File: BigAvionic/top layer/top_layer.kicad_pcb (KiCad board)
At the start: 4 copper layers, 68 x 68 mm, 28 parts, among them J1 Conn_01x08, J2 Conn_Coaxial, J3 Conn_01x04, U1 NEO-M9N-00B, U2 MMC5983MA

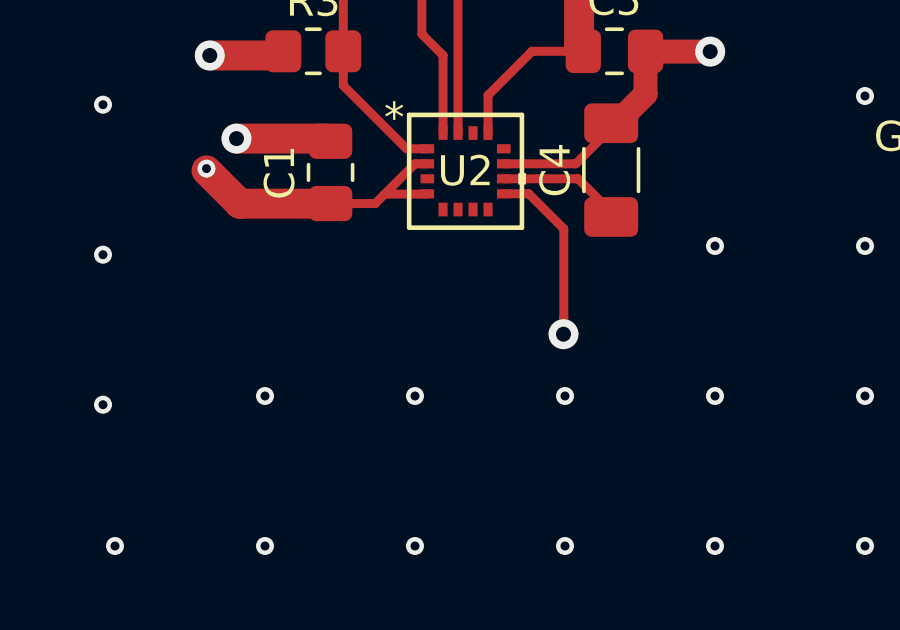
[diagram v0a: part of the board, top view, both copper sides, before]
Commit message: edit some in MCU for production
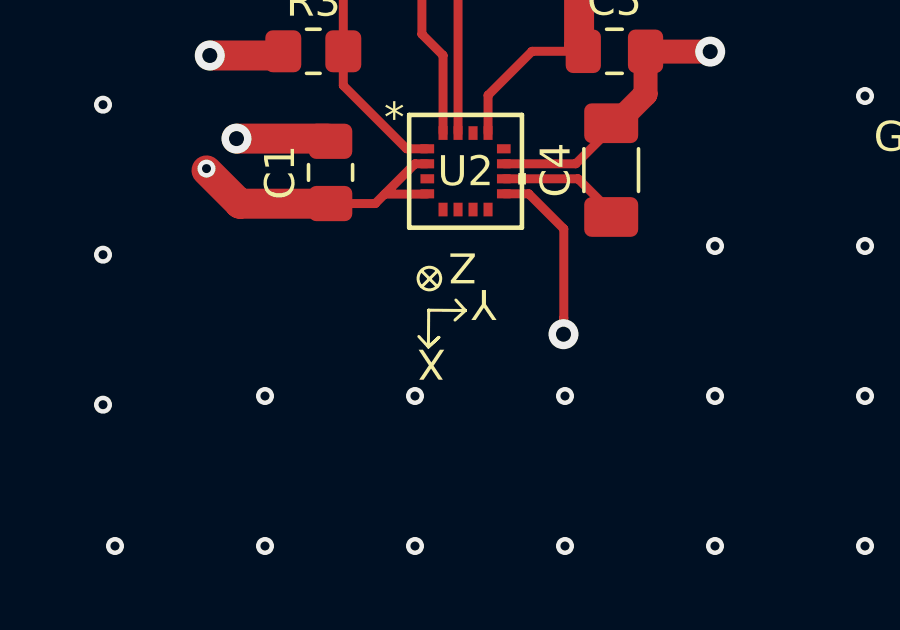
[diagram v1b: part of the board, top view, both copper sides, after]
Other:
- board text added: "X"
- board text added: "Y"
- board text added: "Z"
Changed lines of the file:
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@@
 	)
 	(gr_line
+		(start 125.171691 125.94)
+		(end 123.941691 125.93)
+		(stroke
+			(width 0.1)
+			(type default)
+		)
+		(layer "F.SilkS")
+	)
+	(gr_line
+		(start 125.171691 125.94)
+		(end 124.821691 126.26)
+		(stroke
+			(width 0.1)
+			(type default)
+		)
+		(layer "F.SilkS")
+	)
+	(gr_circle
+		(center 123.969729 124.875)
+		(end 123.619729 124.735)
+		(stroke
+			(width 0.1)
+			(type default)
+		)
+		(fill no)
+		(layer "F.SilkS")
+	)
+	(gr_line
+		(start 123.936691 127.155)
+		(end 123.946691 125.925)
+		(stroke
+			(width 0.1)
+			(type default)
+		)
+		(layer "F.SilkS")
+	)
+	(gr_line
+		(start 123.936691 127.155)
+		(end 123.616691 126.805)
+		(stroke
+			(width 0.1)
+			(type default)
+		)
+		(layer "F.SilkS")
+	)
+	(gr_line
+		(start 123.936691 127.155)
+		(end 124.286691 126.835)
+		(stroke
+			(width 0.1)
+			(type default)
+		)
+		(layer "F.SilkS")
+	)
+	(gr_line
+		(start 123.72 125.14)
+		(end 124.22 124.64)
+		(stroke
+			(width 0.1)
+			(type default)
+		)
+		(layer "F.SilkS")
+	)
+	(gr_line
+		(start 124.23 125.14)
+		(end 123.73 124.64)
+		(stroke
+			(width 0.1)
+			(type default)
+		)
+		(layer "F.SilkS")
+	)
+	(gr_line
+		(start 124.286691 126.835)
+		(end 123.936691 127.155)
+		(stroke
+			(width 0.1)
+			(type default)
+		)
+		(layer "F.SilkS")
+	)
+	(gr_line
+		(start 124.851691 125.59)
+		(end 125.171691 125.94)
+		(stroke
+			(width 0.1)
+			(type default)
+		)
+		(layer "F.SilkS")
+	)
+	(gr_line
 		(start 162.7 73.3)
 		(end 102.7 73.3)
@@
 		(layer "Edge.Cuts")
 	)
+	(gr_text "X"
+		(at 124.506691 127.125 180)
+		(layer "F.SilkS")
+		(effects
+			(font
+				(size 1 1)
+				(thickness 0.1)
+			)
+			(justify left bottom)
+		)
+	)
+	(gr_text "Z"
+		(at 125.546691 123.915 180)
+		(layer "F.SilkS")
+		(effects
+			(font
+				(size 1 1)
+				(thickness 0.1)
+			)
+			(justify left bottom)
+		)
+	)
+	(gr_text "Y\n"
+		(at 126.206691 125.135 180)
+		(layer "F.SilkS")
+		(effects
+			(font
+				(size 1 1)
+				(thickness 0.1)
+			)
+			(justify left bottom)
+		)
+	)
 	(gr_text "S_TOP"
 		(at 158.93 89 0)
@@
 		)
 	)
+	(group ""
+		(members "0b557512-cb73-45e5-a6f4-f902f71d0391" "0c09536f-b48c-4b1f-bfc2-54ec7c9e1c28"
+			"1a738692-3f88-4541-9e03-4c10d2bc8bb1" "1bbe62bf-9ff4-4897-b6ba-afde5a3a1c8d"
+			"201cbc5e-cc5f-4f52-80ec-600e4f7f748f" "3d9b4e09-bb3e-4dd4-8ea1-13a07f475ef4"
+			"45d56f21-34da-464b-9b08-cf18cfdd7c22" "4831d113-8abb-4857-829c-e190f09edcf0"
+			"6de26f78-5829-4643-a000-02dcc94b8266" "7645b6f3-a6f3-4611-9dc1-8f1c7f64191f"
+			"92826094-b3bd-4f3f-9137-d5c5ea98e3b5" "c90d9668-26c9-4bb0-893a-177ce0240573"
+			"d2823234-f236-4bf4-aeaf-3b7e5d2f3b1c"
+		)
+	)
